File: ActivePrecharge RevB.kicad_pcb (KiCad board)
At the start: 2 copper layers, 98.4 x 58.9 mm, 93 parts, among them IC1 AMC1350DWVR, IC2 AMC1350DWVR, IC3 ZXRE160AET5TA, J1 HVConnector, J2 ExportConnector, J3 PrechargeContactor, J4 MainContactor, U1 LT1963AEST-3.3#TRPBF, U2 TLV9001IDBVR, U3 TLV9001IDBVR

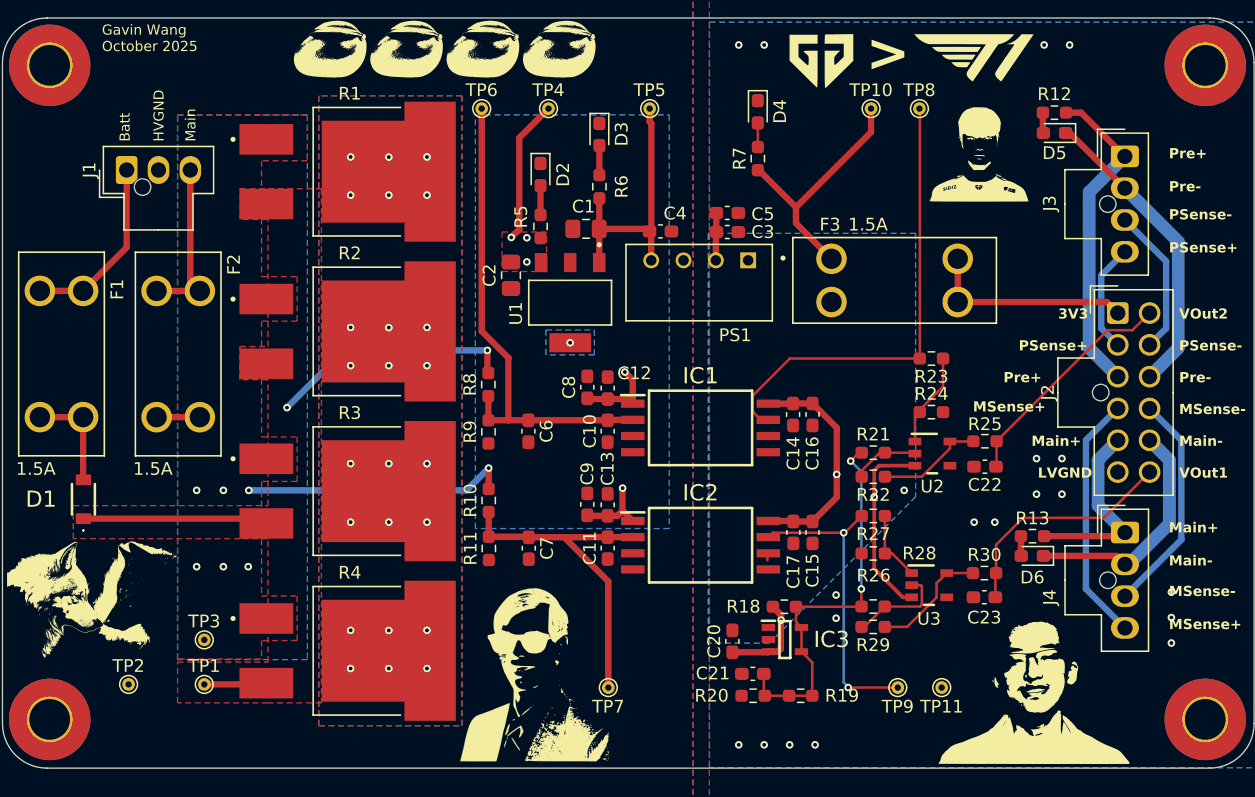
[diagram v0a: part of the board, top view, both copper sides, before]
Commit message: Fixed pin, LED, and connector names being overwritten after updating PCB
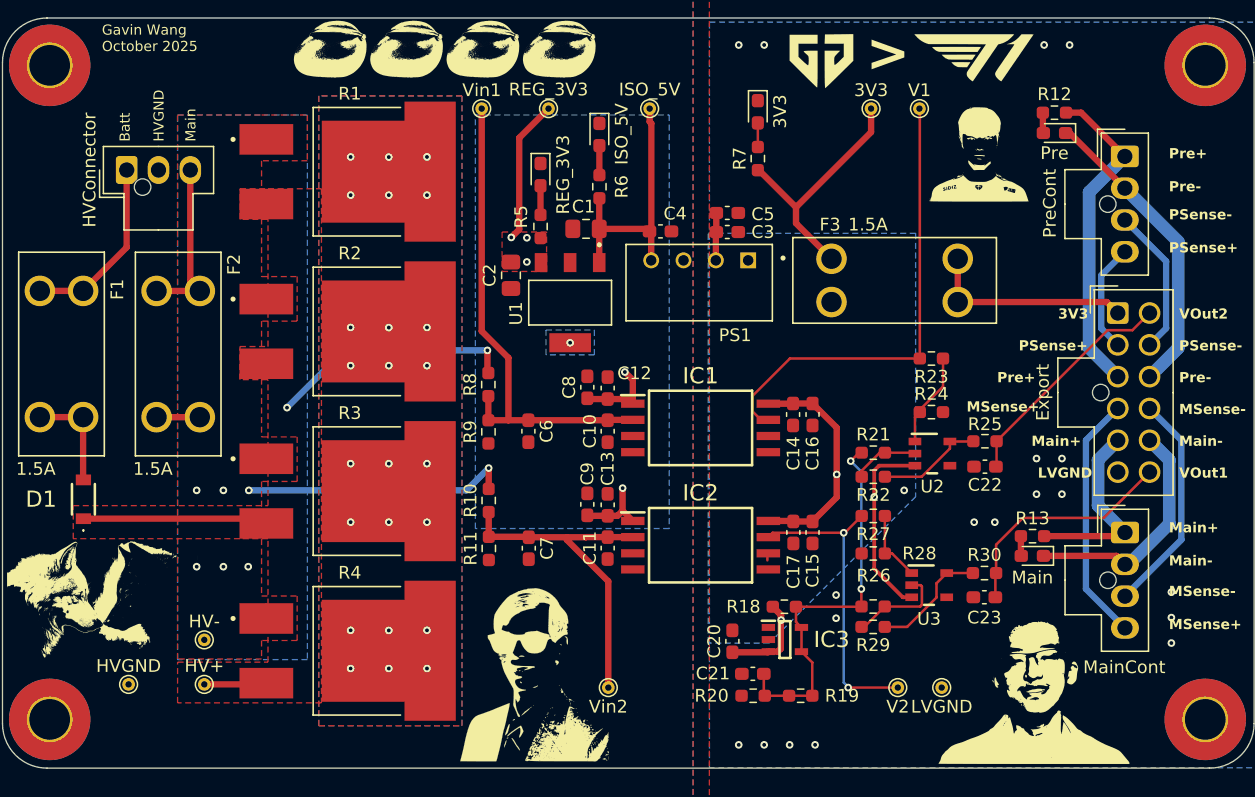
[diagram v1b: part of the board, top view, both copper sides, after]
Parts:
- renumbered TP10 to 3V3, D4 to 3V3, J2 to Export, TP1 to HV+, TP3 to HV-, J1 to HVConnector, TP2 to HVGND, TP5 to ISO_5V, D3 to ISO_5V, TP11 to LVGND, D6 to Main, J4 to MainCont, D5 to Pre, J3 to PreCont, D2 to REG_3V3, TP4 to REG_3V3, TP8 to V1, TP9 to V2, TP6 to Vin1, TP7 to Vin2
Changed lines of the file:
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@@
 		(descr "Molex Nano-Fit Power Connectors, 105309-xx04, 4 Pins per row (http://www.molex.com/pdm_docs/sd/1053091203_sd.pdf), generated with kicad-footprint-generator")
 		(tags "connector Molex Nano-Fit vertical")
-		(property "Reference" "J4"
-			(at -5.905 5.08512 90)
+		(property "Reference" "MainCont"
+			(at -0.05212 10.58512 180)
 			(layer "F.SilkS")
 			(effects
@@
 		(descr "LED SMD 0603 (1608 Metric), square (rectangular) end terminal, IPC-7351 nominal, (Body size source: http://www.tortai-tech.com/upload/download/2011102023233369053.pdf), generated with kicad-footprint-generator")
 		(tags "LED handsolder")
-		(property "Reference" "D2"
+		(property "Reference" "REG_3V3"
 			(at 0 -1.775 90)
 			(layer "F.SilkS")
@@
 		(descr "THT pad as test Point, diameter 1.0mm, hole diameter 0.5mm")
 		(tags "test point THT pad")
-		(property "Reference" "TP11"
+		(property "Reference" "LVGND"
 			(at 0 -1.5 180)
 			(layer "F.SilkS")
@@
 		(descr "THT pad as test Point, diameter 1.0mm, hole diameter 0.5mm")
 		(tags "test point THT pad")
-		(property "Reference" "TP8"
+		(property "Reference" "V1"
 			(at 0 -1.448 0)
 			(layer "F.SilkS")
@@
 		(descr "Molex Nano-Fit Power Connectors, 105310-xx12, 6 Pins per row (http://www.molex.com/pdm_docs/sd/1053101208_sd.pdf), generated with kicad-footprint-generator")
 		(tags "connector Molex Nano-Fit vertical")
-		(property "Reference" "J2"
-			(at -5.48712 6.23512 90)
+		(property "Reference" "Export"
+			(at -5.88712 6.23512 90)
 			(layer "F.SilkS")
 			(effects
@@
 		(descr "THT pad as test Point, diameter 1.0mm, hole diameter 0.5mm")
 		(tags "test point THT pad")
-		(property "Reference" "TP10"
+		(property "Reference" "3V3"
 			(at 0 -1.448 0)
 			(layer "F.SilkS")
@@
 		(descr "THT pad as test Point, diameter 1.0mm, hole diameter 0.5mm")
 		(tags "test point THT pad")
-		(property "Reference" "TP4"
-			(at 0 -1.448 0)
+		(property "Reference" "REG_3V3"
+			(at 0 -1.5 0)
 			(layer "F.SilkS")
 			(effects
@@
 		(descr "THT pad as test Point, diameter 1.0mm, hole diameter 0.5mm")
 		(tags "test point THT pad")
-		(property "Reference" "TP1"
+		(property "Reference" "HV+"
 			(at 0 -1.448 0)
 			(layer "F.SilkS")
@@
 		(descr "LED SMD 0603 (1608 Metric), square (rectangular) end terminal, IPC-7351 nominal, (Body size source: http://www.tortai-tech.com/upload/download/2011102023233369053.pdf), generated with kicad-footprint-generator")
 		(tags "LED handsolder")
-		(property "Reference" "D6"
+		(property "Reference" "Main"
 			(at 0 -1.7 0)
 			(layer "F.SilkS")
@@
 		(descr "THT pad as test Point, diameter 1.0mm, hole diameter 0.5mm")
 		(tags "test point THT pad")
-		(property "Reference" "TP3"
+		(property "Reference" "HV-"
 			(at 0 -1.448 0)
 			(layer "F.SilkS")
@@
 		(descr "THT pad as test Point, diameter 1.0mm, hole diameter 0.5mm")
 		(tags "test point THT pad")
-		(property "Reference" "TP5"
-			(at 0 -1.448 0)
+		(property "Reference" "ISO_5V"
+			(at 0 -1.5 0)
 			(layer "F.SilkS")
 			(effects
@@
 		(descr "THT pad as test Point, diameter 1.0mm, hole diameter 0.5mm")
 		(tags "test point THT pad")
-		(property "Reference" "TP7"
+		(property "Reference" "Vin2"
 			(at 0 -1.5 180)
 			(layer "F.SilkS")
@@
 		(descr "THT pad as test Point, diameter 1.0mm, hole diameter 0.5mm")
 		(tags "test point THT pad")
-		(property "Reference" "TP2"
+		(property "Reference" "HVGND"
 			(at 0 -1.448 0)
 			(layer "F.SilkS")
@@
 				(font
 					(size 1 1)
-					(thickness 0.15)
+					(thickness 0.125)
 				)
 			)
@@
 		(descr "THT pad as test Point, diameter 1.0mm, hole diameter 0.5mm")
 		(tags "test point THT pad")
-		(property "Reference" "TP9"
+		(property "Reference" "V2"
 			(at 0 1.5 0)
 			(layer "F.SilkS")
@@
 		(descr "Molex Nano-Fit Power Connectors, 105309-xx03, 3 Pins per row (http://www.molex.com/pdm_docs/sd/1053091203_sd.pdf), generated with kicad-footprint-generator")
 		(tags "connector Molex Nano-Fit vertical")
-		(property "Reference" "J1"
+		(property "Reference" "HVConnector"
 			(at 0 -2.92 90)
 			(layer "F.SilkS")
@@
 		(descr "Molex Nano-Fit Power Connectors, 105309-xx04, 4 Pins per row (http://www.molex.com/pdm_docs/sd/1053091203_sd.pdf), generated with kicad-footprint-generator")
 		(tags "connector Molex Nano-Fit vertical")
-		(property "Reference" "J3"
+		(property "Reference" "PreCont"
 			(at -5.895 3.69 90)
 			(layer "F.SilkS")
@@
 		(descr "LED SMD 0603 (1608 Metric), square (rectangular) end terminal, IPC-7351 nominal, (Body size source: http://www.tortai-tech.com/upload/download/2011102023233369053.pdf), generated with kicad-footprint-generator")
 		(tags "LED handsolder")
-		(property "Reference" "D3"
+		(property "Reference" "ISO_5V"
 			(at -0.0375 -1.75 90)
 			(layer "F.SilkS")
@@
 		(descr "LED SMD 0603 (1608 Metric), square (rectangular) end terminal, IPC-7351 nominal, (Body size source: http://www.tortai-tech.com/upload/download/2011102023233369053.pdf), generated with kicad-footprint-generator")
 		(tags "LED handsolder")
-		(property "Reference" "D4"
+		(property "Reference" "3V3"
 			(at -0.025 -1.75 90)
 			(layer "F.SilkS")
@@
 		(descr "THT pad as test Point, diameter 1.0mm, hole diameter 0.5mm")
 		(tags "test point THT pad")
-		(property "Reference" "TP6"
+		(property "Reference" "Vin1"
 			(at 0 -1.448 0)
 			(layer "F.SilkS")
@@
 		(descr "LED SMD 0603 (1608 Metric), square (rectangular) end terminal, IPC-7351 nominal, (Body size source: http://www.tortai-tech.com/upload/download/2011102023233369053.pdf), generated with kicad-footprint-generator")
 		(tags "LED handsolder")
-		(property "Reference" "D5"
+		(property "Reference" "Pre"
 			(at 0 -1.58125 0)
 			(layer "F.SilkS")
@@
 	)
 	(gr_text "MSense+"
-		(at 176.4 90.9 0)
+		(at 175.9 90.9 0)
 		(layer "F.SilkS")
 		(effects
@@
 	)
 	(gr_text "Pre+"
-		(at 178.8 88.6 0)
+		(at 178.3 88.6 0)
 		(layer "F.SilkS")
 		(effects

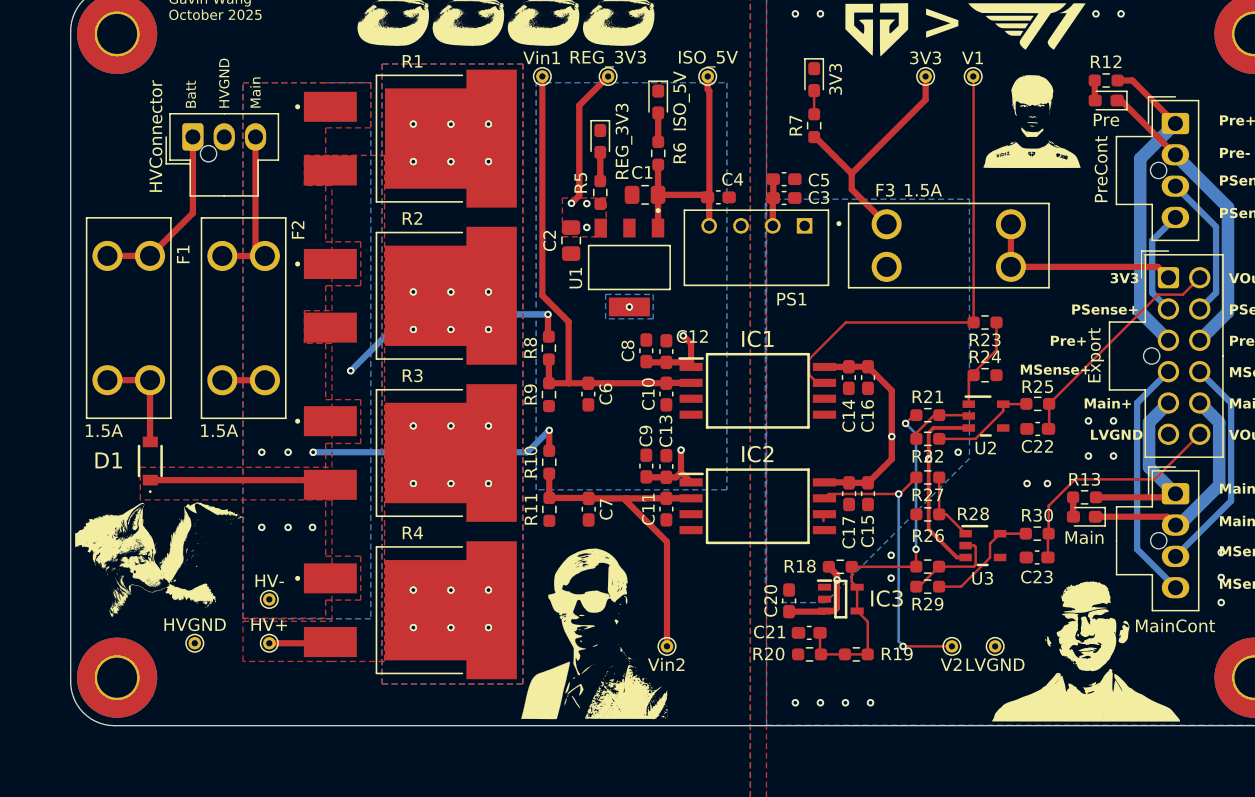
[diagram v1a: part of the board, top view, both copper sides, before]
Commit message: Deleted a redundant via on a thermal pad
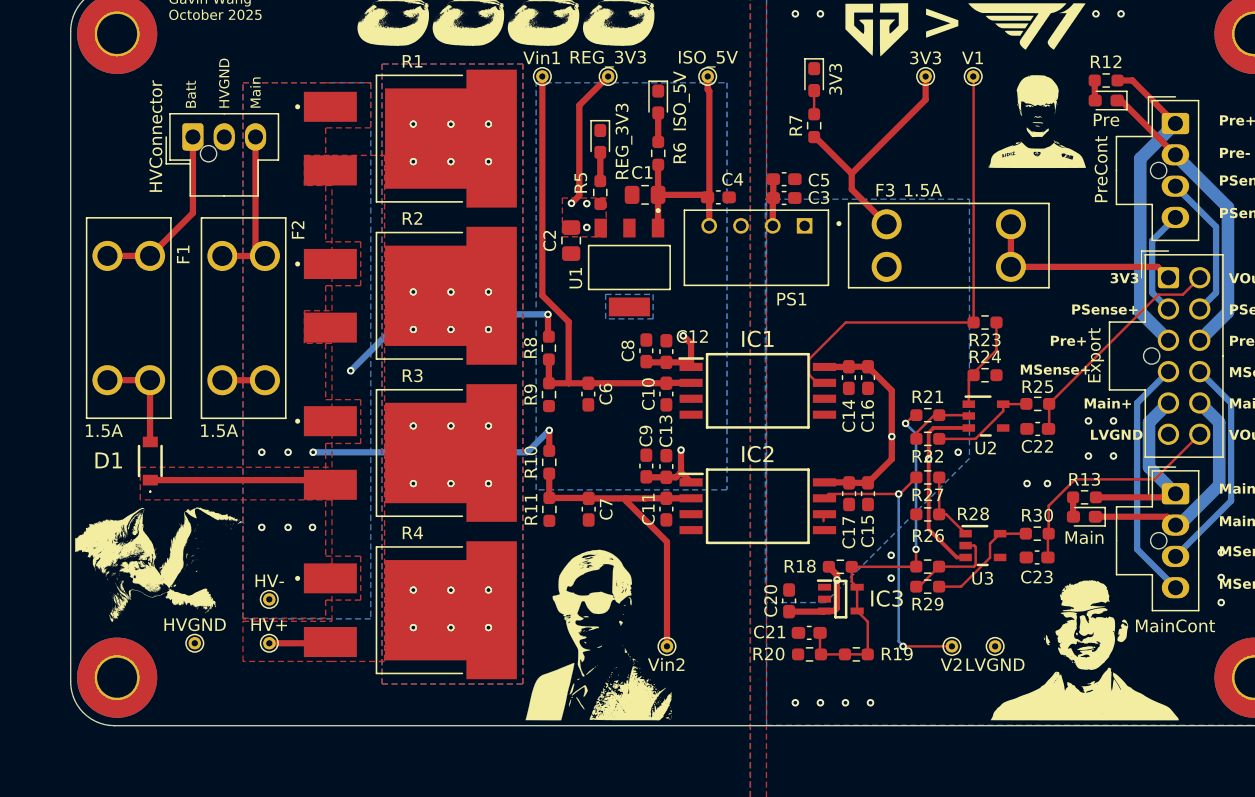
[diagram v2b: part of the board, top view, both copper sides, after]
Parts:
- moved G*** 0.43 mm to (177.0, 70.6)
- moved G*** 0.40 mm to (108.0, 106.1)
- moved LOGO1 0.36 mm to (141.8, 111.4)
- moved G*** 0.14 mm to (181.1, 111.8)
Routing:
- net HVGND: vias 1 -> 0
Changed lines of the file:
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@@
 	(footprint "LOGO"
 		(layer "F.Cu")
-		(at 176.6 70.6)
+		(at 177.031319 70.6)
 		(property "Reference" "G***"
 			(at 0 0 0)
@@
 	(footprint "LOGO"
 		(layer "F.Cu")
-		(at 181.2 111.895084)
+		(at 181.1 111.8)
 		(property "Reference" "G***"
 			(at 0 0 0)
@@
 	(footprint "UTSVT-Logos:Hallock_Image_Tiny"
 		(layer "F.Cu")
-		(at 141.472932 111.319857)
+		(at 141.822932 111.419857)
 		(property "Reference" "LOGO1"
 			(at 0 0 0)
@@
 	(footprint "LOGO"
 		(layer "F.Cu")
-		(at 108 105.7)
+		(at 108 106.1)
 		(property "Reference" "G***"
 			(at 0 0 0)
@@
 		)
 	)
-	(via
-		(at 144.75 85.3996)
-		(size 0.6)
-		(drill 0.3)
-		(layers "F.Cu" "B.Cu")
-		(net 1)
-	)
 	(segment

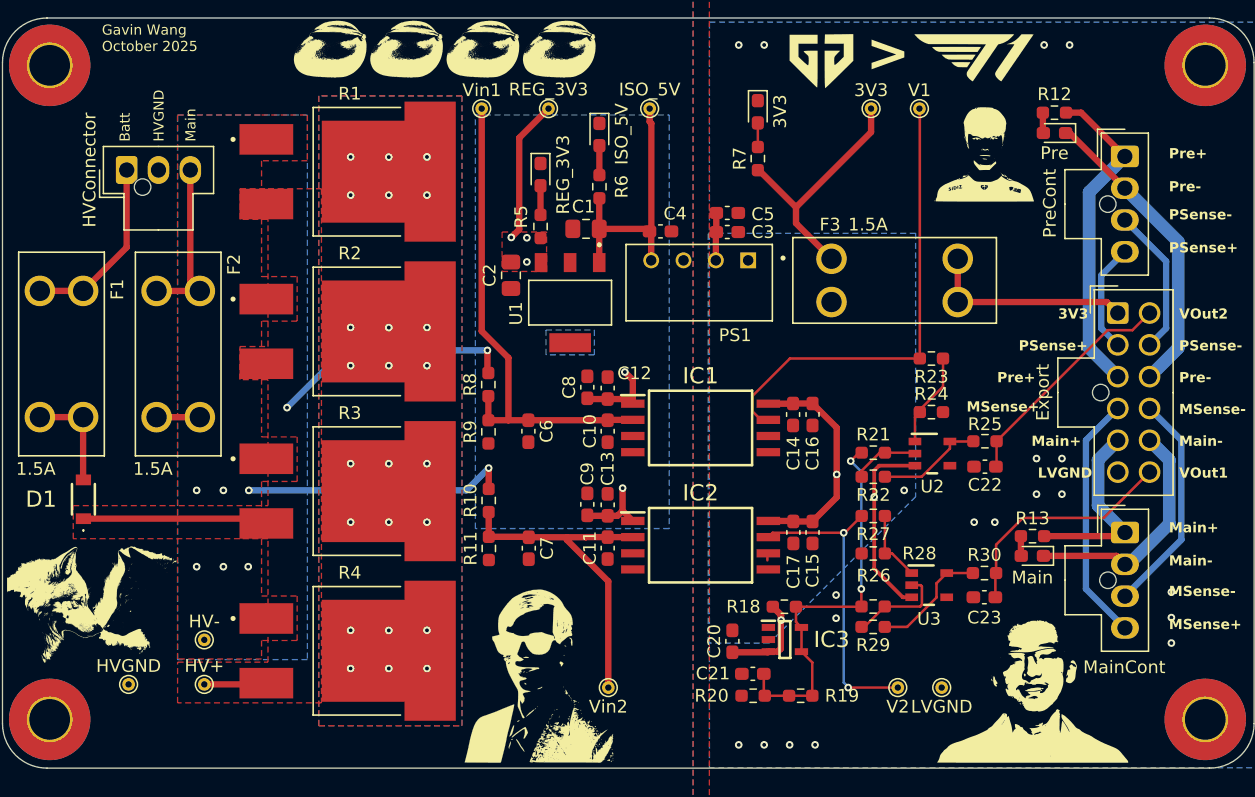
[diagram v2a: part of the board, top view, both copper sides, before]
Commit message: Fixed 0.8V reference circuit short on accidental node for divider side
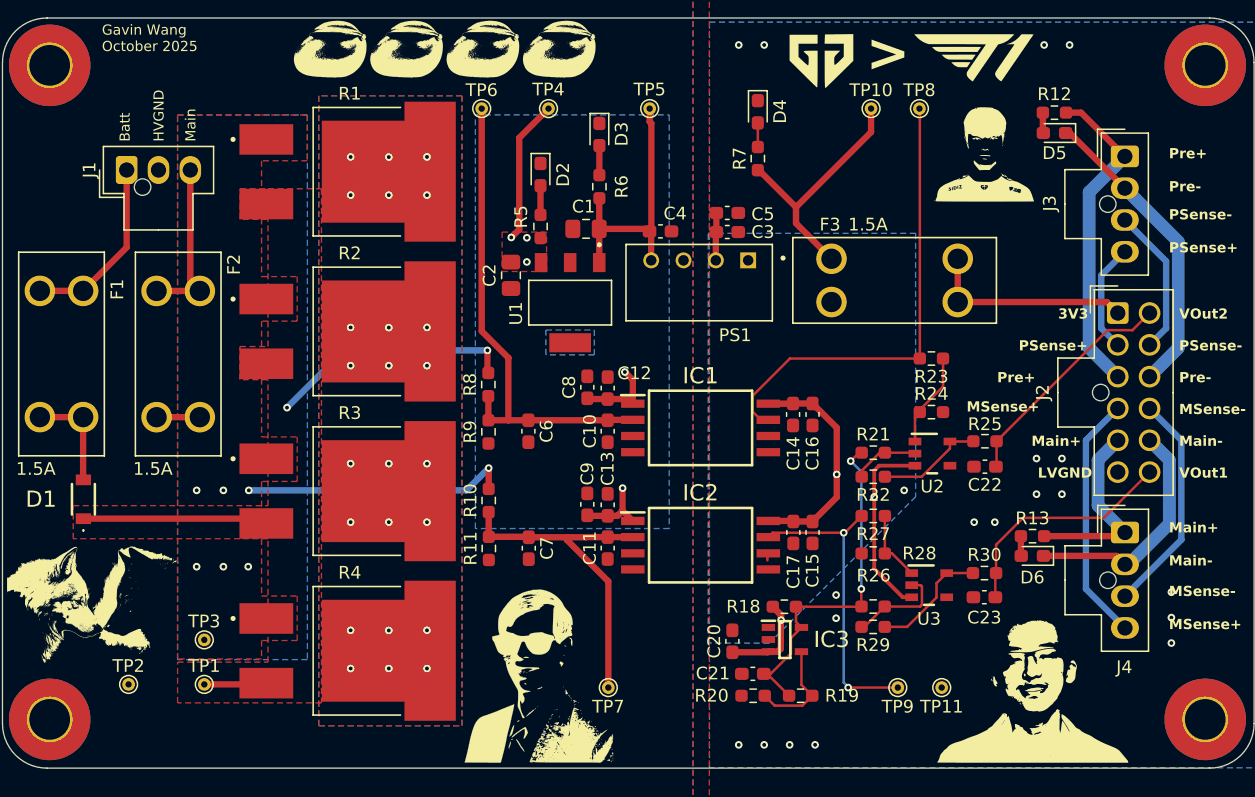
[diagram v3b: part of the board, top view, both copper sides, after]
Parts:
- renumbered REG_3V3 to D2, ISO_5V to D3, 3V3 to D4, Pre to D5, Main to D6, HVConnector to J1, Export to J2, PreCont to J3, MainCont to J4, HV+ to TP1, 3V3 to TP10, LVGND to TP11, HVGND to TP2, HV- to TP3, REG_3V3 to TP4, ISO_5V to TP5, Vin1 to TP6, Vin2 to TP7, V1 to TP8, V2 to TP9
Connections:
- IC3 pad 4: REG_0V8 -> Net-(IC3-FB)
- R19 pad 1: REG_0V8 -> Net-(IC3-FB)
- R20 pad 1: REG_0V8 -> Net-(IC3-FB)
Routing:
- net Net-(IC3-FB): track 0.00 -> 8.30 mm
- net REG_0V8: track 31.1 -> 27.8 mm
